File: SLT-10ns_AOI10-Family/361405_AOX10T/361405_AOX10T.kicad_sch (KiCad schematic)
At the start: 11 parts, among them U1 12-Pin_SLx_Can

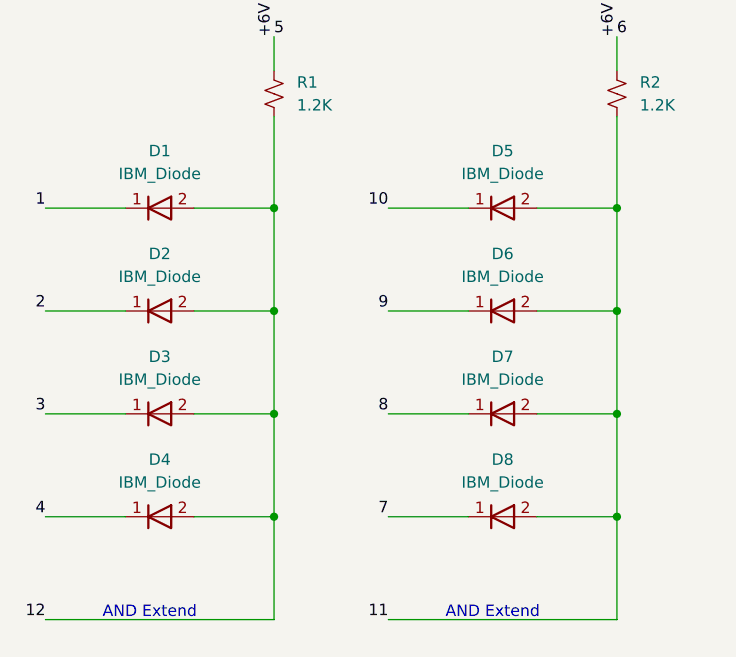
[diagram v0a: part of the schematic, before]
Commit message: Finished off the SLT-30 family of parts, started on the SLT-700 family. Changed labeling of transistors and diodes in all schematics, but have yet to update all the pdf files. This is a TODO...
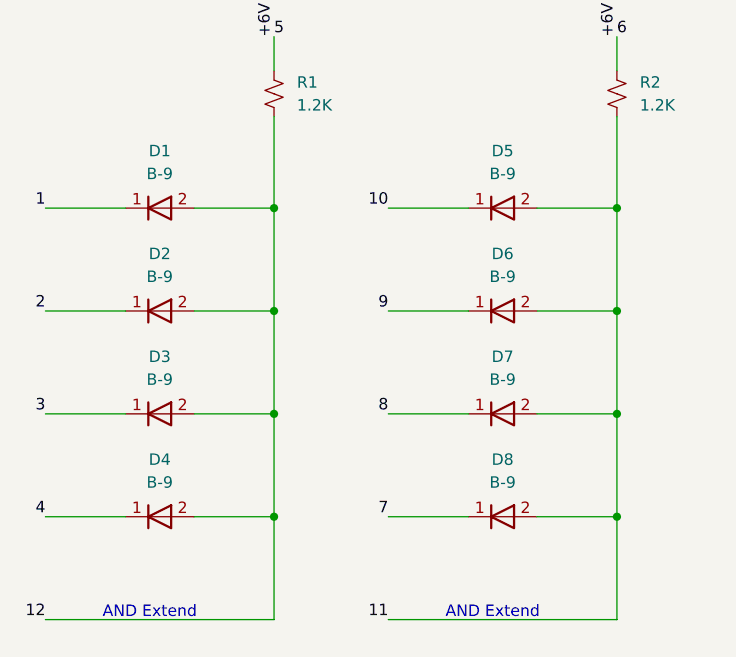
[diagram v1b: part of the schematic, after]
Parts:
- D1, D2, D3, D4, D5, D6, D7, D8: value IBM_Diode -> B-9
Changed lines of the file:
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@@
     (in_bom yes) (on_board yes) (fields_autoplaced)
     (property "Reference" "D4" (id 0) (at 114.3 109.22 0))
-    (property "Value" "IBM_Diode" (id 1) (at 114.3 111.76 0))
+    (property "Value" "B-9" (id 1) (at 114.3 111.76 0))
     (property "Footprint" "Diode_SMD:D_0201_0603Metric" (id 2) (at 114.3 113.03 0)
       (effects (font (size 1.27 1.27)) hide)
@@
     (in_bom yes) (on_board yes) (fields_autoplaced)
     (property "Reference" "D2" (id 0) (at 114.3 86.36 0))
-    (property "Value" "IBM_Diode" (id 1) (at 114.3 88.9 0))
+    (property "Value" "B-9" (id 1) (at 114.3 88.9 0))
     (property "Footprint" "Diode_SMD:D_0201_0603Metric" (id 2) (at 114.3 90.17 0)
       (effects (font (size 1.27 1.27)) hide)
@@
     (in_bom yes) (on_board yes) (fields_autoplaced)
     (property "Reference" "D7" (id 0) (at 152.4 97.79 0))
-    (property "Value" "IBM_Diode" (id 1) (at 152.4 100.33 0))
+    (property "Value" "B-9" (id 1) (at 152.4 100.33 0))
     (property "Footprint" "Diode_SMD:D_0201_0603Metric" (id 2) (at 152.4 101.6 0)
       (effects (font (size 1.27 1.27)) hide)
@@
     (in_bom yes) (on_board yes) (fields_autoplaced)
     (property "Reference" "D1" (id 0) (at 114.3 74.93 0))
-    (property "Value" "IBM_Diode" (id 1) (at 114.3 77.47 0))
+    (property "Value" "B-9" (id 1) (at 114.3 77.47 0))
     (property "Footprint" "Diode_SMD:D_0201_0603Metric" (id 2) (at 114.3 78.74 0)
       (effects (font (size 1.27 1.27)) hide)
@@
     (in_bom yes) (on_board yes) (fields_autoplaced)
     (property "Reference" "D8" (id 0) (at 152.4 109.22 0))
-    (property "Value" "IBM_Diode" (id 1) (at 152.4 111.76 0))
+    (property "Value" "B-9" (id 1) (at 152.4 111.76 0))
     (property "Footprint" "Diode_SMD:D_0201_0603Metric" (id 2) (at 152.4 113.03 0)
       (effects (font (size 1.27 1.27)) hide)
@@
     (in_bom yes) (on_board yes) (fields_autoplaced)
     (property "Reference" "D3" (id 0) (at 114.3 97.79 0))
-    (property "Value" "IBM_Diode" (id 1) (at 114.3 100.33 0))
+    (property "Value" "B-9" (id 1) (at 114.3 100.33 0))
     (property "Footprint" "Diode_SMD:D_0201_0603Metric" (id 2) (at 114.3 101.6 0)
       (effects (font (size 1.27 1.27)) hide)
@@
     (in_bom yes) (on_board yes) (fields_autoplaced)
     (property "Reference" "D5" (id 0) (at 152.4 74.93 0))
-    (property "Value" "IBM_Diode" (id 1) (at 152.4 77.47 0))
+    (property "Value" "B-9" (id 1) (at 152.4 77.47 0))
     (property "Footprint" "Diode_SMD:D_0201_0603Metric" (id 2) (at 152.4 78.74 0)
       (effects (font (size 1.27 1.27)) hide)
@@
     (in_bom yes) (on_board yes) (fields_autoplaced)
     (property "Reference" "D6" (id 0) (at 152.4 86.36 0))
-    (property "Value" "IBM_Diode" (id 1) (at 152.4 88.9 0))
+    (property "Value" "B-9" (id 1) (at 152.4 88.9 0))
     (property "Footprint" "Diode_SMD:D_0201_0603Metric" (id 2) (at 152.4 90.17 0)
       (effects (font (size 1.27 1.27)) hide)
@@
   (symbol_instances
     (path "/801d24ff-be6b-468d-a51b-7691568aa1d6"
-      (reference "D1") (unit 1) (value "IBM_Diode") (footprint "Diode_SMD:D_0201_0603Metric")
+      (reference "D1") (unit 1) (value "B-9") (footprint "Diode_SMD:D_0201_0603Metric")
     )
     (path "/15a433c4-0335-46e4-884c-814357806383"
-      (reference "D2") (unit 1) (value "IBM_Diode") (footprint "Diode_SMD:D_0201_0603Metric")
+      (reference "D2") (unit 1) (value "B-9") (footprint "Diode_SMD:D_0201_0603Metric")
     )
     (path "/b60d9340-c16c-48dd-8b20-3b5943f6c8ab"
-      (reference "D3") (unit 1) (value "IBM_Diode") (footprint "Diode_SMD:D_0201_0603Metric")
+      (reference "D3") (unit 1) (value "B-9") (footprint "Diode_SMD:D_0201_0603Metric")
     )
     (path "/096216c5-6902-43a5-8004-8a4114c8baa4"
-      (reference "D4") (unit 1) (value "IBM_Diode") (footprint "Diode_SMD:D_0201_0603Metric")
+      (reference "D4") (unit 1) (value "B-9") (footprint "Diode_SMD:D_0201_0603Metric")
     )
     (path "/e1f12525-18b0-44bc-a18d-820be7b9946e"
-      (reference "D5") (unit 1) (value "IBM_Diode") (footprint "Diode_SMD:D_0201_0603Metric")
+      (reference "D5") (unit 1) (value "B-9") (footprint "Diode_SMD:D_0201_0603Metric")
     )
     (path "/e5207290-41d1-4708-be96-2b2603b0ffee"
-      (reference "D6") (unit 1) (value "IBM_Diode") (footprint "Diode_SMD:D_0201_0603Metric")
+      (reference "D6") (unit 1) (value "B-9") (footprint "Diode_SMD:D_0201_0603Metric")
     )
     (path "/1be5506a-07a3-447d-b379-4e04e402bbb9"
-      (reference "D7") (unit 1) (value "IBM_Diode") (footprint "Diode_SMD:D_0201_0603Metric")
+      (reference "D7") (unit 1) (value "B-9") (footprint "Diode_SMD:D_0201_0603Metric")
     )
     (path "/8e4b9e6c-d9b9-437f-9616-3123e2a2c38e"
-      (reference "D8") (unit 1) (value "IBM_Diode") (footprint "Diode_SMD:D_0201_0603Metric")
+      (reference "D8") (unit 1) (value "B-9") (footprint "Diode_SMD:D_0201_0603Metric")
     )
     (path "/512fd277-9de7-454a-b3d9-ab06f52cae1a"
